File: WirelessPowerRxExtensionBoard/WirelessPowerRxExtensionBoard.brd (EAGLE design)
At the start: 50.9 x 51 mm, 37 parts, among them Q1 MOSFET-N, Q2 MOSFET-N, Q3 MOSFET-N

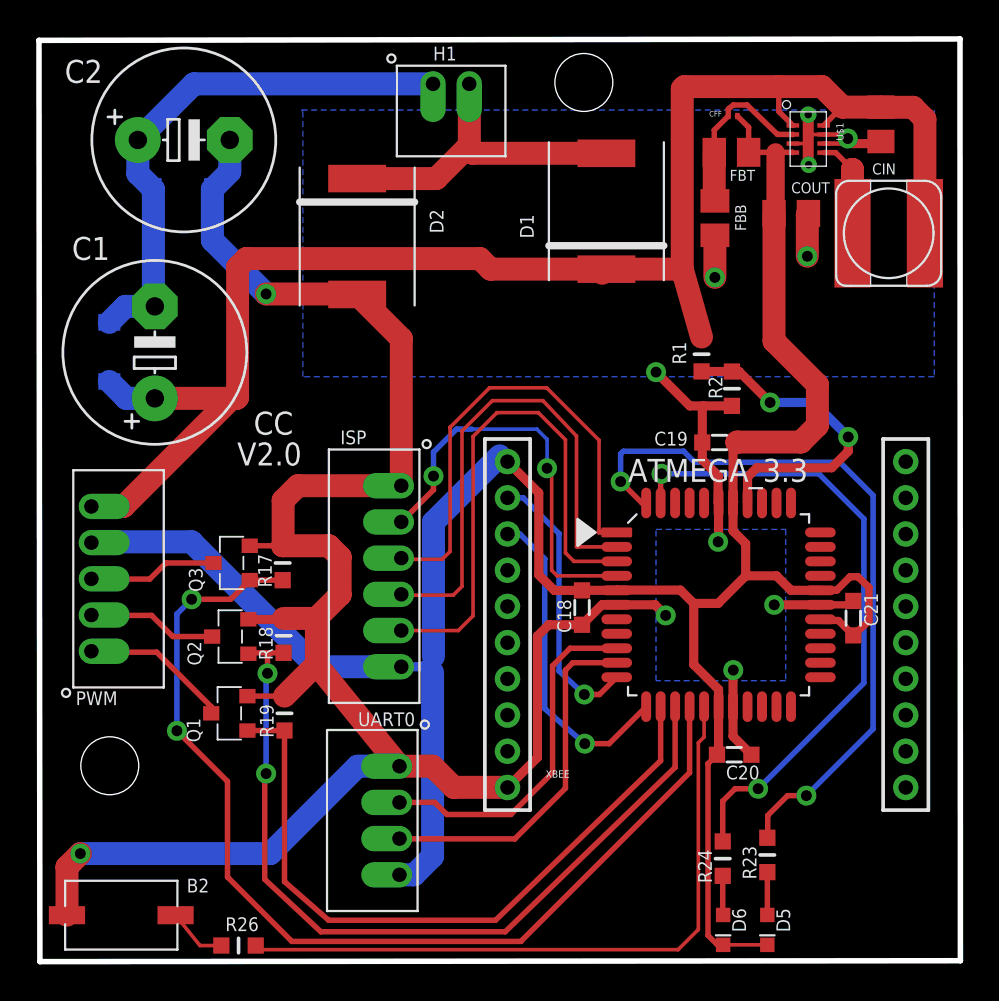
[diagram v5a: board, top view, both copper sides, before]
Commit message: Second Rerouting Revision Complete
Extended Ground plane across entire board, switched Voltage regulator
feedback resistors to 0603
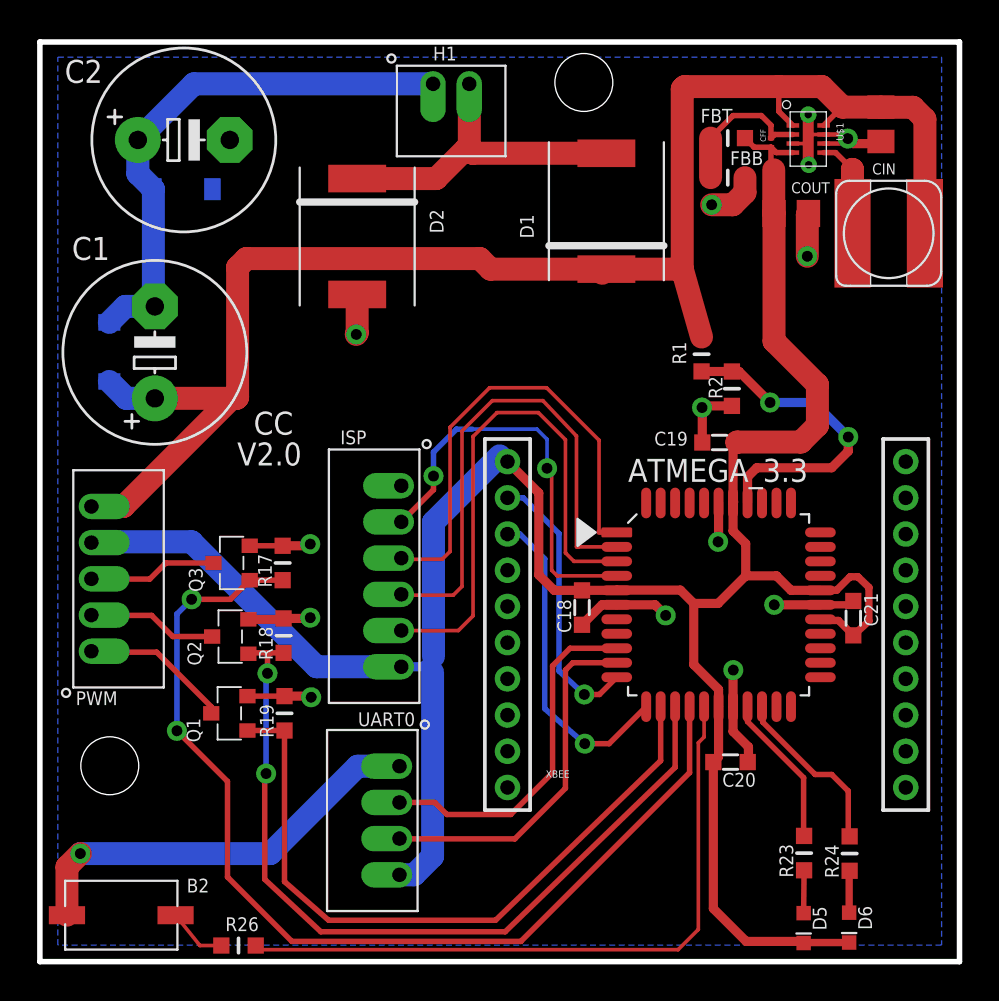
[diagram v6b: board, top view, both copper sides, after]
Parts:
- FBB: value 287K -> 287k; device resistor:M0805 -> carrick:R0603
- FBT: value 499K -> 499k; device resistor:M0805 -> carrick:R0603
- moved R24 7.02 mm to (44.7, 5.97)
- moved D6 6.96 mm to (44.7, 1.88)
- moved CFF 2.57 mm to (40.4, 45.2), turned to 90 degrees
- moved FBB 2.35 mm to (38.0, 43.3), turned to 180 degrees
- moved R23 2.03 mm to (42.2, 5.99)
- moved D5 2.01 mm to (42.2, 1.85)
- moved FBT 0.81 mm to (38.0, 45.5)
- moved C20 0.45 mm to (38.2, 11.0)
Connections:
- net 3.3V: now also FBT.P$2; no longer FBT.2
- net AT3_LED1: now also ATMEGA_3.3.19; no longer ATMEGA_3.3.44
- net AT3_LED2: now also ATMEGA_3.3.20; no longer ATMEGA_3.3.43
- net FB: now also FBB.P$2, FBT.P$1; no longer FBB.2, FBT.1
- net GND: now also FBB.P$1; no longer FBB.1
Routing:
- net GND: track 144.3 -> 69.3 mm, vias 12 -> 15
- net AT3_LED1: track 40.4 -> 8.44 mm, vias 2 -> 0
- net AT3_LED2: track 35.7 -> 9.76 mm, vias 2 -> 0
- net 3.3V: track 137.0 -> 138.8 mm
- net FB: track 9.72 -> 8.27 mm
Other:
- board size 50.9 x 51 mm -> 50.8 x 50.8 mm
